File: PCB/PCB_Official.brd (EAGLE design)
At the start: 160 x 100 mm, 66 parts, among them IC1 MCP73871, U1 TPS63070, U2 STM32F767ZIT6, U3 STM32L053C8T6, U4 TPS63070, U5 BATTERY-MANAGEMENT-TEMP_BQ274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

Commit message: Schematic almost finalized
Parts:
- added C23, C24: 2.2uF, rcl:C0805
- added C25: 10nF, rcl:C0805
- added C26, C27, C28, C29, C30, C31, C32, C33, C34, C35, C36, C37, C43, C44, C45, C46, C47: 100nF, rcl:C0805
- added C38: 4.7uF, rcl:C0805
- added C39, C40, C41, C42: 4.3pF, rcl:C0805
- added C48: 1uF, rcl:C0805
- added J3: 455-1750-1-ND, SparkFun-Connectors:1X03
- added Q1: 220mA/50V/3.5Ω, SparkFun-DiscreteSemi:SOT23-3
- added R21, R22, R23, R24: 10k, rcl:R0805
- added SOLAR: (no value), adafruit:JST-PH-2-SMT-RA
- J1: device SparkFun-Connectors:1X11 -> SparkFun-Connectors:1X13
- moved J1 51.3 mm to (143.5, 36.8), turned to 90 degrees
- moved R3 13.9 mm to (47.0, 61.0), turned to 270 degrees
- moved J2 12.7 mm to (112.4, 76.2), turned to 180 degrees
- moved PWR 1.27 mm to (27.9, 67.9), turned to 90 degrees
- moved U3 0.90 mm to (71.8, 55.2), turned to 180 degrees
- moved DONE 0.63 mm to (24.1, 67.9), turned to 90 degrees
- turned CHRG/LBO to 270 degrees
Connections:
- removed net N$32: J1.4
- removed net PDR_ON: U2.143
- removed net VCAP_1: U2.71
- removed net VCAP_2: U2.106
- removed net VDD: U2.108, U2.131, U2.144, U2.17, U2.30, U2.39, U2.52, U2.62, U2.72, U2.84
- removed net VDDA: U2.33
- removed net VDDSDMMC: U2.121
- removed net VDDUSB: U2.95
- removed net VREFP: U2.32
- new net DCMI_D2: J1.5, U2.98
- new net DCMI_D3: J1.6, U2.99
- new net DCMI_D4: J1.7, U2.112
- new net DCMI_D5: J1.8, U2.117
- new net DCMI_D6: J1.9, U2.139
- new net DCMI_D7: J1.10, U2.140
- new net DCMI_VSYNC: J1.11, U2.124
- new net F7_RX: MCU_UART.4, U2.35
- new net F7_TX: MCU_UART.2, U2.34
- new net GSM_RST: U$1.P$2, U3.41
- new net I2C_SCL: J1.13, U2.136
- new net I2C_SDA: J1.12, U2.137
- new net L0_RX: MCU_UART.1, U3.22
- new net L0_SWCLK: L0_PROGRAM.3, U3.37
- new net L0_SWDIO: L0_PROGRAM.2, U3.34
- new net L0_TX: MCU_UART.3, U3.21
- new net LORA_INT: U$9.G0, U3.42
- new net LORA_RST: U$9.PRST, U3.43
- new net MCU_RST: J2.4, L0_PROGRAM.4, U2.25, U3.7
- new net SYS_JTCK_SWCLK: J2.3, U2.109
- new net SYS_JTMS_SWDIO: J2.2, U2.105
- new net TIM3_CH2: Q1.2, R22.1
- new net VCAP1: C23.1, U2.71
- new net VCAP2: C24.1, U2.106
- net +3V3: now also C25.1, C26.1, C27.1, C28.1, C29.1, C30.1, C31.1, C32.1, C33.1, C34.1, C35.1, C36.1, C37.1, C38.1, C43.1, C44.1, C45.1, C46.1, C47.1, C48.1, J2.5, L0_PROGRAM.5, Q1.1, R22.2, U2.108, U2.121, U2.131, U2.143, U2.144, U2.17, U2.30, U2.32, U2.33, U2.39, U2.52, U2.6, U2.62, U2.72, U2.84, U2.95, U3.36, U3.9
- net +5V: now also J3.1, R23.2
- net BAT_SCL: now also U3.45
- net BAT_SDA: now also U3.46
- net DCMI_D1: now also J1.4
- net GND: now also C23.2, C24.2, C25.2, C26.2, C27.2, C28.2, C29.2, C30.2, C31.2, C32.2, C33.2, C34.2, C35.2, C36.2, C37.2, C38.2, C39.2, C40.2, C41.2, C42.2, C43.2, C44.2, C45.2, C46.2, C47.2, C48.2, J2.1, J3.3, L0_PROGRAM.1, R21.2, R24.1, SOLAR.2; no longer U$9.PRST
- net N$23: now also R21.1, U2.138; no longer J1.11
- net N$24: now also R24.2, U3.44; no longer J1.10
- net N$27: now also C40.1, U2.24; no longer J1.9
- net N$28: now also C39.1, U2.23; no longer J1.8
- net N$29: now also J3.2, Q1.3, R23.1; no longer J1.7
- net N$30: now also C42.1, U3.6; no longer J1.6
- net N$31: now also C41.1, U3.5; no longer J1.5
- net VBAT: no longer U2.6
- net VCC: now also SOLAR.1

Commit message: Pre-midpoint design review.
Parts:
- removed C4: 0.1uF, SparkFun-Capacitors:0603
- removed D2: RED, SparkFun-LED:LED-0603
- removed J1: (no value), SparkFun-Connectors:1X13
- removed R13: 2K, adafruit:0805-THM
- removed R3: 10k, SparkFun-Resistors:0603
- removed R4: 365k, SparkFun-Resistors:0603
- removed R6: 1k, SparkFun-Resistors:0603
- removed THERM: 10K, adafruit:0805-THM
- added C50: 10uF, adafruit:C0805
- added C51: 0.1uF, rcl:C0603
- added J4: (no value), SparkFun-Connectors:1X16
- added R25: 10k, adafruit:R0805
- added R26, R27: 10k, rcl:R0603
- added R28: 68.1k, rcl:R0603
- added R29: 213k, rcl:R0603
- added R30: 1k, rcl:R0603
- added RED, RED1: RED, microbuilder:CHIPLED_0805_NOOUTLINE
- added U$2, U$3: 8MHZ_OSC, ForestVisionParts:8MHZ_OSC
- C1, C18: value 0.1uF -> 10uF; device SparkFun-Capacitors:0603 -> adafruit:C0805
- C12, C13, C15, C16, C17, C2, C3, C6: device SparkFun-Capacitors:0805 -> adafruit:C0805
- C14: device SparkFun-Capacitors:0603 -> rcl:C0603
- C19: value 10uF -> 4700uF/10V; device SparkFun-Capacitors:0805 -> ForestVisionParts:ADAFRUIT_E5-13
- C20: value 10uF -> 0.1uF; device SparkFun-Capacitors:0805 -> rcl:C0603
- C5, C9: value 10uF -> 22uF; device SparkFun-Capacitors:0805 -> adafruit:C0805
- C7: value 22uF -> 0.1uF; device SparkFun-Capacitors:0805 -> rcl:C0603
- C8: value 22uF -> 10uF; device SparkFun-Capacitors:0805 -> adafruit:C0805
- D1: value RED -> MBR120VLSFT1GOSCT; device SparkFun-LED:LED-0603 -> ForestVisionParts:MICROBUILDER_SOD-123
- MCU_UART: device SparkFun-Connectors:JST-4-PTH -> pinhead:1X04
- R1: value 10k -> 2k; device SparkFun-Resistors:0603 -> adafruit:R0805
- R17: value 1k -> 10k; device SparkFun-Resistors:0603 -> rcl:R0603
- R18: value 10k -> 68.1k; device SparkFun-Resistors:0603 -> rcl:R0603
- R19: value 213k -> 365k; device rcl:R0805 -> rcl:R0603
- R2: value 68.1k -> 10k; device SparkFun-Resistors:0603 -> adafruit:R0805
- R20: value 10k -> 1k; device rcl:R0805 -> rcl:R0603
- R5: value 68.1k -> 10k; device SparkFun-Resistors:0603 -> rcl:R0603
- R7: device SparkFun-Resistors:0603 -> adafruit:R0805
- moved R23 300.8 mm to (115.6, 83.2), turned to 90 degrees
- moved R22 290.1 mm to (106.7, 81.3), turned to 90 degrees
- moved Q1 288.4 mm to (111.1, 81.9), turned to 270 degrees
- moved C48 260.1 mm to (59.1, 33.0), turned to 90 degrees
- moved SOLAR 259.3 mm to (12.1, 62.2), turned to 90 degrees
- moved C46 256.2 mm to (69.2, 28.6), turned to 90 degrees
- moved C47 251.5 mm to (56.5, 28.6), turned to 90 degrees
- moved C38 245.3 mm to (109.9, 28.6), flipped to the bottom
- moved C37 243.4 mm to (118.7, 15.2)
- moved C42 238.9 mm to (69.8, 24.1), turned to 90 degrees
- moved C44 235.8 mm to (64.1, 14.6), flipped to the bottom, turned to 270 degrees
- moved C43 235.3 mm to (66.7, 15.9), turned to 270 degrees
- moved C45 234.2 mm to (53.3, 17.8), turned to 180 degrees
- moved C41 232.2 mm to (69.8, 19.1), turned to 270 degrees
- moved C39 231.6 mm to (89.5, 27.9), turned to 90 degrees
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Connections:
- removed net GND_CHARGER: C10.2
- new net CLK_TBD: J4.15
- new net N$32: D1.A, SOLAR.1
- net !EN: now also R17.1; no longer R1.1
- net !EN1: now also R27.1; no longer R3.1
- net +3V3: now also C18.1, J4.16, R29.2, R30.2, R7.2; no longer C19.1, R17.2, R19.2
- net +5V: now also C3.1, C9.1, R19.2, R20.2; no longer C7.1, C8.1, R4.2, R6.2
- net DCMI_D0: now also J4.4; no longer J1.3
- net DCMI_D1: now also J4.5; no longer J1.4
- net DCMI_D2: now also J4.6; no longer J1.5
- net DCMI_D3: now also J4.7; no longer J1.6
- net DCMI_D4: now also J4.8; no longer J1.7
- net DCMI_D5: now also J4.9; no longer J1.8
- net DCMI_D6: now also J4.10; no longer J1.9
- net DCMI_D7: now also J4.11; no longer J1.10
- net DCMI_HSYNC: now also J4.2; no longer J1.1
- net DCMI_PIXCLK: now also J4.3; no longer J1.2
- net DCMI_VSYNC: now also J4.12; no longer J1.11
- net F7_RX: now also MCU_UART.1; no longer MCU_UART.4
- net F7_TX: now also MCU_UART.3; no longer MCU_UART.2
- net GND: now also C10.2, C19.-, C50.2, C51.2, J4.1, R1.1, R18.1, R25.1, R28.1, RED.C, RED1.C; no longer C19.2, C4.2, D1.C, D2.C, R13.1, R20.1, R5.1, THERM.1
- net GPOUT: now also R7.1
- net I2C_SCL: now also J4.13; no longer J1.13
- net I2C_SDA: now also J4.14; no longer J1.12
- net L0_RX: now also MCU_UART.4; no longer MCU_UART.1
- net L0_TX: now also MCU_UART.2; no longer MCU_UART.3
- net N$17: now also R1.2; no longer R13.2
- net N$19: now also R2.2; no longer THERM.2
- net N$20: now also R30.1, RED.A; no longer D2.A, R17.1
- net N$21: now also R28.2, R29.1; no longer R19.1, R5.2
- net N$26: now also R25.2; no longer R20.2
- net N$27: now also U$2.P$2
- net N$28: now also U$2.P$1
- net N$30: now also U$3.P$2
- net N$31: now also U$3.P$1
- net N$4: now also R18.2, R19.1; no longer R2.2, R4.1
- net N$5: now also R20.1, RED1.A; no longer D1.A, R6.1
- net N$6: now also C14.1; no longer C4.1
- net N$9: now also C20.1; no longer C14.1
- net PS: now also R5.1; no longer R7.1
- net PS1: now also R26.1; no longer R18.1
- net TIM3_CH2: now also U2.135
- net VCC: now also C19.+, D1.C; no longer SOLAR.1
- net VOUT_CHARGER: now also C50.1, C51.1, C7.1, C8.1, R17.2, R26.2, R27.2, R5.2; no longer C18.1, C20.1, C3.1, C9.1, R1.2, R18.2, R3.2, R7.2
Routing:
- net +3V3: track 0.00 -> 148.0 mm, vias 0 -> 32
- net +5V: track 0.00 -> 103.5 mm
- net MCU_RST: track 0.00 -> 81.9 mm, vias 0 -> 4
- net RX_GSM: track 0.00 -> 80.7 mm, vias 0 -> 3
- net TX_GSM: track 0.00 -> 79.2 mm, vias 0 -> 1
- net VCC: track 0.00 -> 79.2 mm, vias 0 -> 4
- net GSM_RST: track 0.00 -> 69.6 mm, vias 0 -> 2
- net VOUT_CHARGER: track 0.00 -> 61.8 mm, vias 0 -> 3
- net BAT_SDA: track 0.00 -> 57.3 mm, vias 0 -> 4
- net DCMI_PIXCLK: track 0.00 -> 54.7 mm, vias 0 -> 4
- net DCMI_HSYNC: track 0.00 -> 50.9 mm, vias 0 -> 2
- net BAT_SCL: track 0.00 -> 50.7 mm, vias 0 -> 2
- net TIM3_CH2: track 0.00 -> 50.1 mm, vias 0 -> 2
- net I2C_SDA: track 0.00 -> 49.1 mm
- net I2C_SCL: track 0.00 -> 47.5 mm
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- added copper zone on layer 1, net +3V3
- added copper zone on layer 16, net +3V3
- added copper zone on layer 1, net +5V
- added copper zone on layer 1, net GND
- added copper zone on layer 1, net N$1
- added copper zone on layer 1, net N$2
- added copper zone on layer 1, net N$7
- added copper zone on layer 1, net N$8
- added copper zone on layer 1, net VBAT
- added copper zone on layer 1, net VCC
- added copper zone on layer 1, net VOUT_CHARGER
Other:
- board size 160 x 100 mm -> 139.7 x 101.6 mm

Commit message: Major revision after design review
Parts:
- removed SOLAR: (no value), adafruit:JST-PH-2-SMT-RA
- added CN1: (no value), adafruit:DCJACK_2MM_PTH
- moved J2 46.8 mm to (66.3, 45.5), turned to 270 degrees
- moved C25 43.5 mm to (83.3, 48.1), turned to 90 degrees
- moved J4 43.2 mm to (104.8, 56.3), turned to 180 degrees
- moved C37 43.1 mm to (90.9, 48.1), turned to 90 degrees
- moved C24 38.5 mm to (72.5, 39.9), turned to 270 degrees
- moved R22 38.2 mm to (68.6, 79.2)
- moved J3 38.2 mm to (81.3, 82.4)
- moved Q1 38.2 mm to (73.0, 79.9)
- moved R23 38.2 mm to (77.5, 81.2)
- moved C23 35.1 mm to (94.7, 41.8), turned to 0 degrees
- moved C38 34.0 mm to (77.6, 39.2), turned to 270 degrees
- moved C28 33.1 mm to (73.8, 36.1), turned to 180 degrees
- moved C12 32.8 mm to (33.9, 44.8)
- moved C20 32.8 mm to (41.3, 36.8)
- moved L2 32.8 mm to (37.8, 46.1)
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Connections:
- new net LORA_EN: U$9.EN, U3.30
- net BAT_SCL: now also U3.21; no longer U3.45
- net BAT_SDA: now also U3.22; no longer U3.46
- net GND: now also CN1.GND, CN1.GNDBREAK; no longer SOLAR.2
- net GSM_RST: now also U3.14; no longer U3.41
- net L0_RX: now also U3.43; no longer U3.22
- net L0_TX: now also U3.42; no longer U3.21
- net LORA_INT: now also U3.29; no longer U3.42
- net LORA_RST: no longer U3.43
- net N$32: now also CN1.PWR; no longer SOLAR.1
- net RX_GSM: now also U3.13; no longer U3.30
- net TX_GSM: now also U3.12; no longer U3.31
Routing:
- net +5V: track 103.5 -> 19.3 mm
- net DCMI_PIXCLK: track 54.7 -> 0.00 mm, vias 4 -> 0
- net DCMI_HSYNC: track 50.9 -> 0.00 mm, vias 2 -> 0
- net I2C_SDA: track 49.1 -> 0.00 mm
- net I2C_SCL: track 47.5 -> 0.00 mm
- net TIM3_CH2: track 50.1 -> 3.71 mm, vias 2 -> 0
- net DCMI_D7: track 44.6 -> 0.00 mm, vias 2 -> 0
- net DCMI_D6: track 42.2 -> 0.00 mm, vias 2 -> 0
- net +3V3: track 148.0 -> 110.1 mm
- net VOUT_CHARGER: track 61.8 -> 25.3 mm
- net LORA_RST: track 34.4 -> 0.00 mm, vias 2 -> 0
- net DCMI_VSYNC: track 33.5 -> 0.03 mm, vias 2 -> 0
- net DCMI_D5: track 26.7 -> 0.00 mm
- net BAT_SDA: track 57.3 -> 32.3 mm, vias 4 -> 0
- net DCMI_D4: track 24.7 -> 0.00 mm, vias 2 -> 0
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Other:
- board size 139.7 x 101.6 mm -> 100 x 100 mm

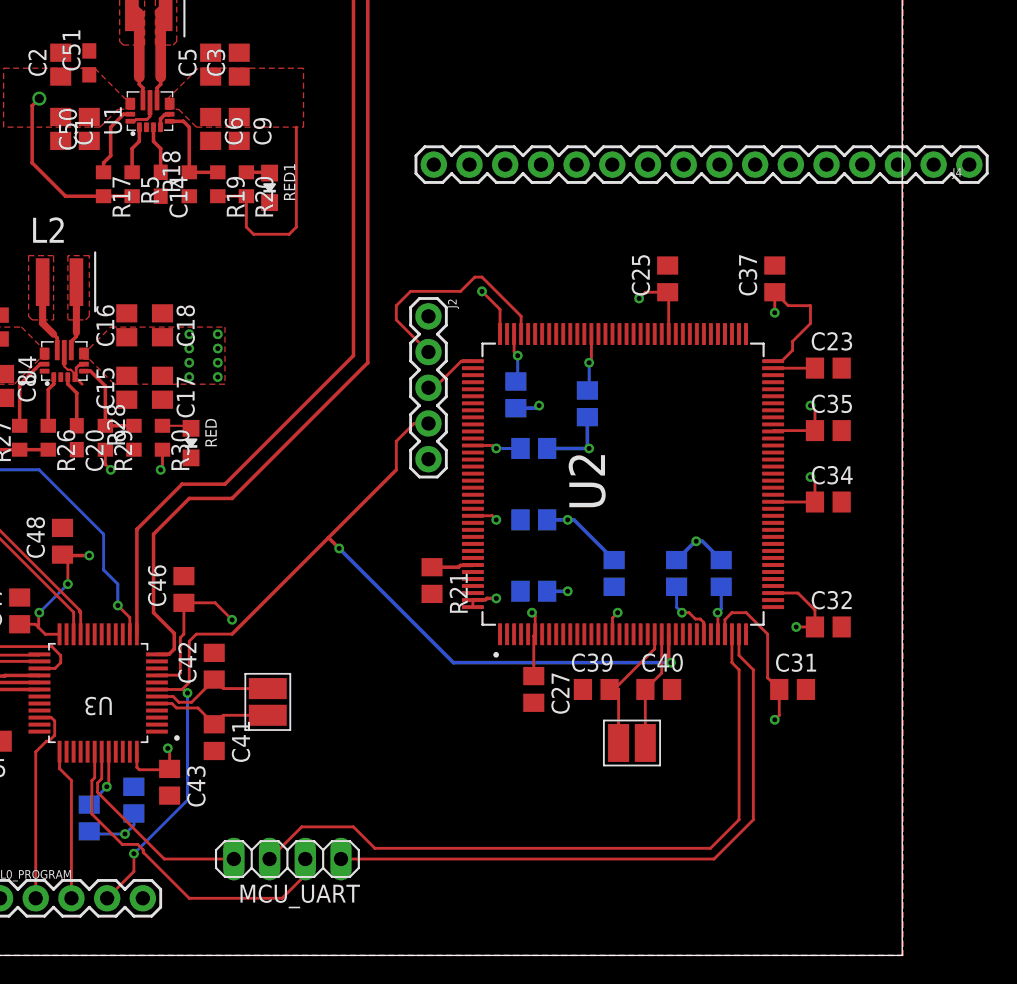
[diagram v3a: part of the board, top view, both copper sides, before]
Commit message: Shuffled pin assignments for AI MCU
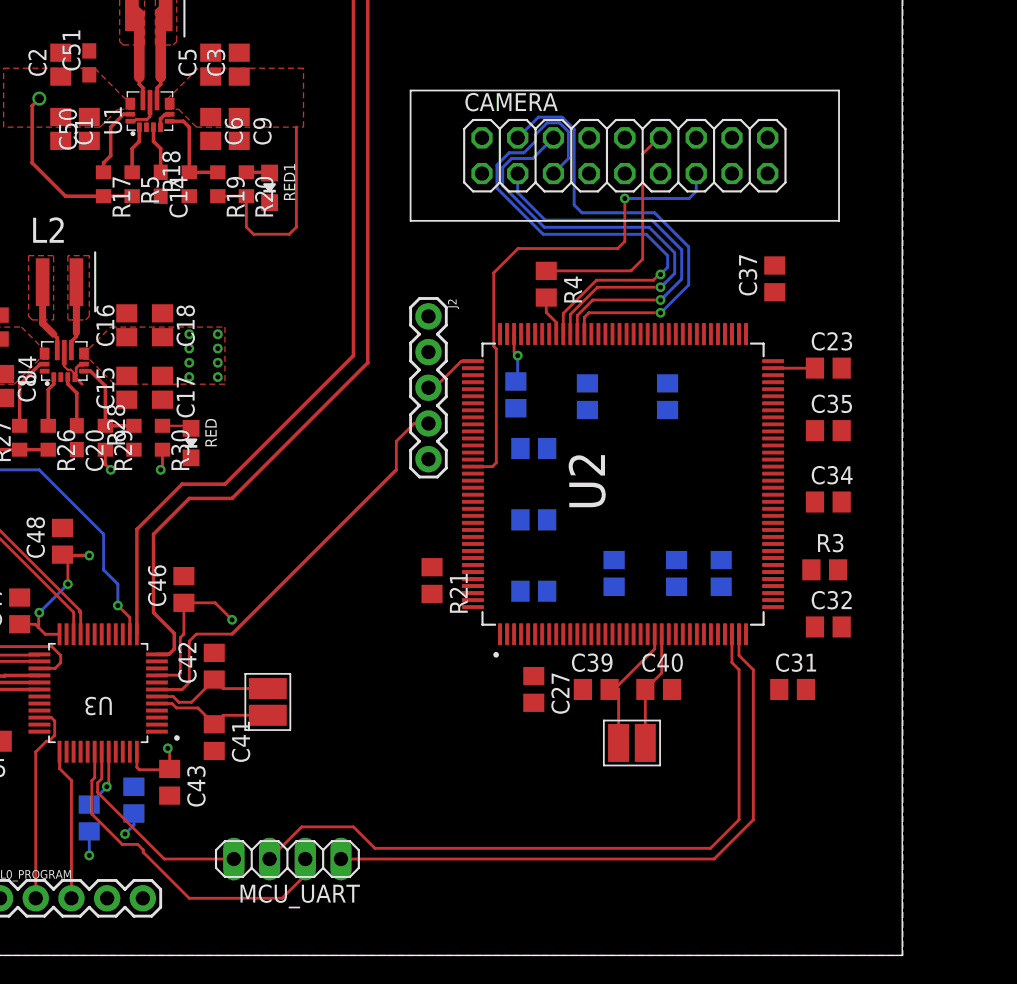
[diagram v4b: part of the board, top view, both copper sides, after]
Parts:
- removed J4: (no value), SparkFun-Connectors:1X16
- added CAMERA: TST-109-02-X-D, ForestVisionParts:TST-109-02-X-D
- added R3, R4: ???, rcl:R0805
- moved FRAME3 118.3 mm to (21.1, -10.7)
- moved C25 8.38 mm to (83.3, 39.8), flipped to the bottom, turned to 270 degrees
- moved C38 0.51 mm to (77.6, 39.8)
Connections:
- removed net CLK_TBD: J4.15
- removed net I2C_SCL: J4.13, U2.136
- removed net I2C_SDA: J4.14, U2.137
- new net CAM_PWDN: CAMERA.2
- new net CAM_RET: CAMERA.1
- new net CAM_SCL: CAMERA.15, U2.81
- new net CAM_SDA: CAMERA.16, U2.82
- new net CAM_XCLK: R4.2, U2.100
- new net N$33: CAMERA.11, R3.2
- new net N$34: CAMERA.12, R4.1
- net +3V3: now also CAMERA.17; no longer J4.16
- net DCMI_D0: now also CAMERA.4, U2.96; no longer J4.4, U2.101
- net DCMI_D1: now also CAMERA.3, U2.97; no longer J4.5, U2.102
- net DCMI_D2: now also CAMERA.6; no longer J4.6
- net DCMI_D3: now also CAMERA.5; no longer J4.7
- net DCMI_D4: now also CAMERA.8; no longer J4.8
- net DCMI_D5: now also CAMERA.7; no longer J4.9
- net DCMI_D6: now also CAMERA.10; no longer J4.10
- net DCMI_D7: now also CAMERA.9; no longer J4.11
- net DCMI_HSYNC: now also CAMERA.14; no longer J4.2
- net DCMI_PIXCLK: now also R3.1; no longer J4.3
- net DCMI_VSYNC: now also CAMERA.13; no longer J4.12
- net GND: now also CAMERA.18; no longer J4.1
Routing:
- net +3V3: track 110.1 -> 37.7 mm, vias 32 -> 17
- net MCU_RST: track 77.6 -> 30.1 mm, vias 4 -> 0
- net DCMI_D3: track 0.00 -> 37.1 mm, vias 0 -> 1
- net DCMI_VSYNC: track 0.03 -> 35.2 mm, vias 0 -> 1
- net DCMI_D0: track 0.00 -> 32.0 mm, vias 0 -> 1
- net DCMI_D2: track 0.00 -> 31.5 mm, vias 0 -> 1
- net DCMI_D1: track 0.00 -> 26.6 mm, vias 0 -> 1
- net GND: track 42.4 -> 23.1 mm, vias 6 -> 2
- net N$34: track 0.00 -> 16.4 mm
- net SYS_JTMS_SWDIO: track 16.4 -> 0.00 mm
- net N$23: track 2.97 -> 0.00 mm
- net CAM_XCLK: track 0.00 -> 2.89 mm
